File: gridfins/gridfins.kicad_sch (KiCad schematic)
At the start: 51 parts, among them J1 RBUS, U1 ESP32-S3, Y1 R940000171

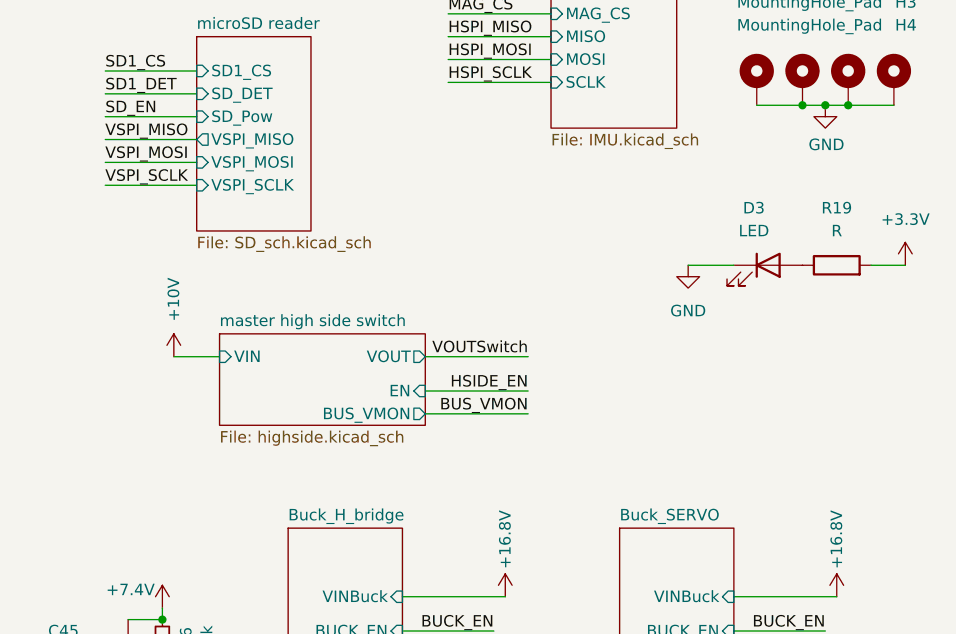
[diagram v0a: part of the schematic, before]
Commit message: PCB + schematic updates
Solved footprint error which prevented PCB from updating

Deleted old buck converter PCB design (old buck now replaced with 2 for servo and linear acc)

Moved Snubber and crossed out capacitor network to the backside of board

Unsure whether if the +10V routing is valid - currently connected via tracers, not planes (may be a problem for current)

Restructured old pcb which previously had planes associated with no nets (assigned nets to them)

If current design approved, will proceed to carry out the same design for the servo controlling buck converter.
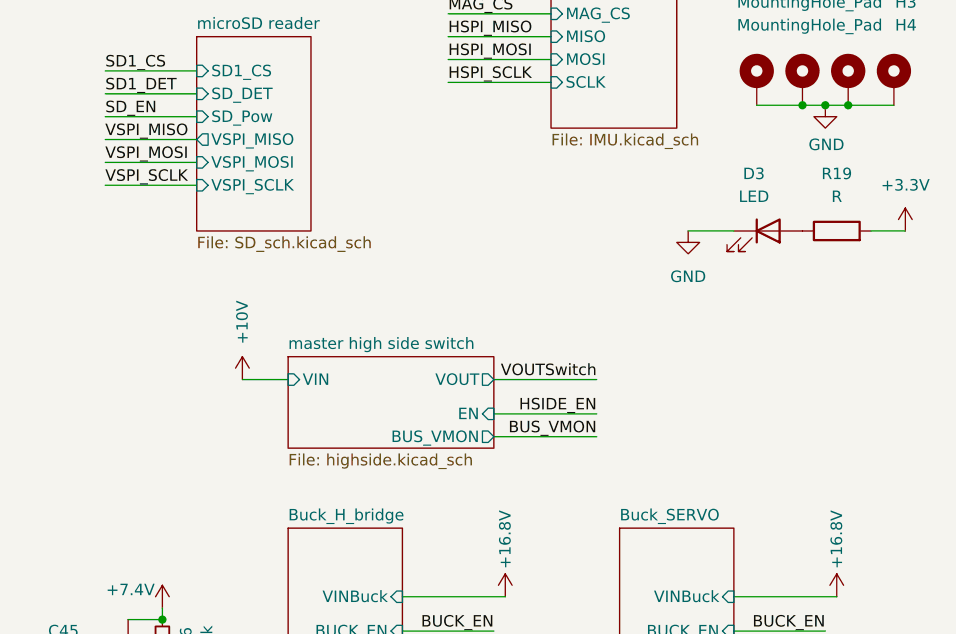
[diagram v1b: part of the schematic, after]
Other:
- moved on the sheet: D3, R19
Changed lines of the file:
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@@
 	(wire
 		(pts
-			(xy 226.06 67.31) (xy 237.49 67.31)
+			(xy 233.68 69.85) (xy 245.11 69.85)
 		)
 		(stroke
@@
 	(wire
 		(pts
-			(xy 255.27 50.8) (xy 260.35 50.8)
+			(xy 255.27 46.99) (xy 260.35 46.99)
 		)
 		(stroke
@@
 	(wire
 		(pts
-			(xy 226.06 60.96) (xy 237.49 60.96)
+			(xy 233.68 63.5) (xy 245.11 63.5)
 		)
 		(stroke
@@
 	(wire
 		(pts
-			(xy 279.4 50.8) (xy 275.59 50.8)
+			(xy 279.4 46.99) (xy 275.59 46.99)
 		)
 		(stroke
@@
 	(wire
 		(pts
-			(xy 198.12 60.96) (xy 203.2 60.96)
+			(xy 205.74 63.5) (xy 210.82 63.5)
 		)
 		(stroke
@@
 	(wire
 		(pts
-			(xy 226.06 64.77) (xy 237.49 64.77)
+			(xy 233.68 67.31) (xy 245.11 67.31)
 		)
 		(stroke
@@
 	)
 	(label "BUS_VMON"
-		(at 237.49 67.31 180)
+		(at 245.11 69.85 180)
 		(effects
 			(font
@@
 	)
 	(label "VOUTSwitch"
-		(at 237.49 60.96 180)
+		(at 245.11 63.5 180)
 		(effects
 			(font
@@
 	)
 	(label "HSIDE_EN"
-		(at 237.49 64.77 180)
+		(at 245.11 67.31 180)
 		(effects
 			(font
@@
 	(symbol
 		(lib_id "power:+3.3V")
-		(at 279.4 50.8 0)
+		(at 279.4 46.99 0)
 		(unit 1)
 		(exclude_from_sim no)
@@
 		(fields_autoplaced yes)
 		(property "Reference" "#PWR028"
-			(at 279.4 54.61 0)
+			(at 279.4 50.8 0)
 			(effects
 				(font
@@
 		)
 		(property "Value" "+3.3V"
-			(at 279.4 45.72 0)
+			(at 279.4 41.91 0)
 			(effects
 				(font
@@
 		)
 		(property "Footprint" ""
-			(at 279.4 50.8 0)
+			(at 279.4 46.99 0)
 			(effects
 				(font
@@
 		)
 		(property "Datasheet" ""
-			(at 279.4 50.8 0)
+			(at 279.4 46.99 0)
 			(effects
 				(font
@@
 		)
 		(property "Description" "Power symbol creates a global label with name \"+3.3V\""
-			(at 279.4 50.8 0)
+			(at 279.4 46.99 0)
 			(effects
 				(font
@@
 	(symbol
 		(lib_id "Device:R")
-		(at 271.78 50.8 90)
+		(at 271.78 46.99 90)
 		(unit 1)
 		(exclude_from_sim no)
@@
 		(dnp no)
 		(property "Reference" "R19"
-			(at 271.78 44.45 90)
+			(at 271.78 40.64 90)
 			(effects
 				(font
@@
 		)
 		(property "Value" "R"
-			(at 271.78 46.99 90)
+			(at 271.78 43.18 90)
 			(effects
 				(font
@@
 		)
 		(property "Footprint" "Resistor_SMD:R_0402_1005Metric"
-			(at 271.78 52.578 90)
+			(at 271.78 48.768 90)
 			(effects
 				(font
@@
 		)
 		(property "Datasheet" "~"
-			(at 271.78 50.8 0)
+			(at 271.78 46.99 0)
 			(effects
 				(font
@@
 		)
 		(property "Description" "Resistor"
-			(at 271.78 50.8 0)
+			(at 271.78 46.99 0)
 			(effects
 				(font
@@
 	(symbol
 		(lib_id "power:+12V")
-		(at 198.12 60.96 0)
+		(at 205.74 63.5 0)
 		(mirror y)
 		(unit 1)
@@
 		(dnp no)
 		(property "Reference" "#PWR062"
-			(at 198.12 64.77 0)
+			(at 205.74 67.31 0)
 			(effects
 				(font
@@
 		)
 		(property "Value" "+10V"
-			(at 198.12 54.61 90)
+			(at 205.74 57.15 90)
 			(effects
 				(font
@@
 		)
 		(property "Footprint" ""
-			(at 198.12 60.96 0)
+			(at 205.74 63.5 0)
 			(effects
 				(font
@@
 		)
 		(property "Datasheet" ""
-			(at 198.12 60.96 0)
+			(at 205.74 63.5 0)
 			(effects
 				(font
@@
 		)
 		(property "Description" "Power symbol creates a global label with name \"+12V\""
-			(at 198.12 60.96 0)
+			(at 205.74 63.5 0)
 			(effects
 				(font
@@
 	(symbol
 		(lib_id "power:GND")
-		(at 255.27 50.8 0)
+		(at 255.27 46.99 0)
 		(unit 1)
 		(exclude_from_sim no)
@@
 		(fields_autoplaced yes)
 		(property "Reference" "#PWR016"
-			(at 255.27 57.15 0)
+			(at 255.27 53.34 0)
 			(effects
 				(font
@@
 		)
 		(property "Value" "GND"
-			(at 255.27 55.88 0)
+			(at 255.27 52.07 0)
 			(effects
 				(font
@@
 		)
 		(property "Footprint" ""
-			(at 255.27 50.8 0)
+			(at 255.27 46.99 0)
 			(effects
 				(font
@@
 		)
 		(property "Datasheet" ""
-			(at 255.27 50.8 0)
+			(at 255.27 46.99 0)
 			(effects
 				(font
@@
 		)
 		(property "Description" "Power symbol creates a global label with name \"GND\" , ground"
-			(at 255.27 50.8 0)
+			(at 255.27 46.99 0)
 			(effects
 				(font
@@
 	(symbol
 		(lib_id "Device:LED")
-		(at 264.16 50.8 0)
+		(at 264.16 46.99 0)
 		(unit 1)
 		(exclude_from_sim no)
@@
 		(dnp no)
 		(property "Reference" "D3"
-			(at 262.5725 44.45 0)
+			(at 262.5725 40.64 0)
 			(effects
 				(font
@@
 		)
 		(property "Value" "LED"
-			(at 262.5725 46.99 0)
+			(at 262.5725 43.18 0)
 			(effects
 				(font
@@
 		)
 		(property "Footprint" "LED_SMD:LED_0402_1005Metric"
-			(at 264.16 50.8 0)
+			(at 264.16 46.99 0)
 			(effects
 				(font
@@
 		)
 		(property "Datasheet" "~"
-			(at 264.16 50.8 0)
+			(at 264.16 46.99 0)
 			(effects
 				(font
@@
 		)
 		(property "Description" "Light emitting diode"
-			(at 264.16 50.8 0)
+			(at 264.16 46.99 0)
 			(effects
 				(font
@@
 		)
 		(property "Sim.Pins" "1=K 2=A"
-			(at 264.16 50.8 0)
+			(at 264.16 46.99 0)
 			(effects
 				(font
@@
 	)
 	(sheet
-		(at 203.2 58.42)
+		(at 210.82 60.96)
 		(size 22.86 10.16)
 		(exclude_from_sim no)
@@
 		)
 		(property "Sheetname" "master high side switch"
-			(at 203.2 57.7084 0)
+			(at 210.82 60.2484 0)
 			(effects
 				(font
@@
 		)
 		(property "Sheetfile" "highside.kicad_sch"
-			(at 203.2 69.1646 0)
+			(at 210.82 71.7046 0)
 			(effects
 				(font
@@
 		)
 		(pin "BUS_VMON" output
-			(at 226.06 67.31 0)
+			(at 233.68 69.85 0)
 			(effects
 				(font
@@
 		)
 		(pin "EN" input
-			(at 226.06 64.77 0)
+			(at 233.68 67.31 0)
 			(effects
 				(font
@@
 		)
 		(pin "VIN" input
-			(at 203.2 60.96 180)
+			(at 210.82 63.5 180)
 			(effects
 				(font
@@
 		)
 		(pin "VOUT" output
-			(at 226.06 60.96 0)
+			(at 233.68 63.5 0)
 			(effects
 				(font

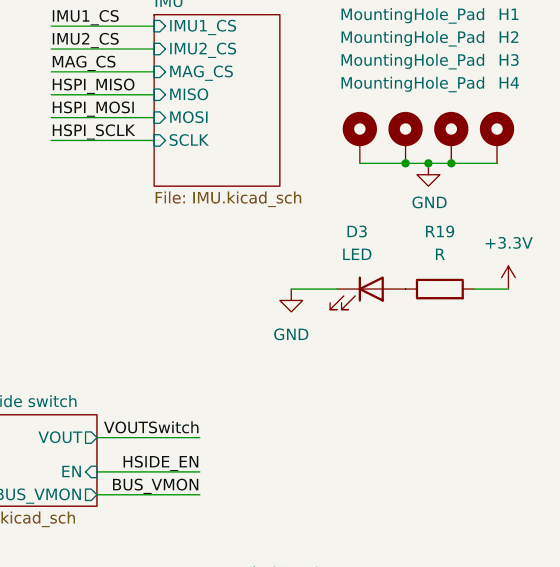
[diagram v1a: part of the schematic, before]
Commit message: Handoff
implemented changes advised by Will. Still a bit unsure about how the EPAD should be connected to ground. The PCB design of both buck converters for servo and Hbridge(linear accuator) was completed - but still needs to be reviewed
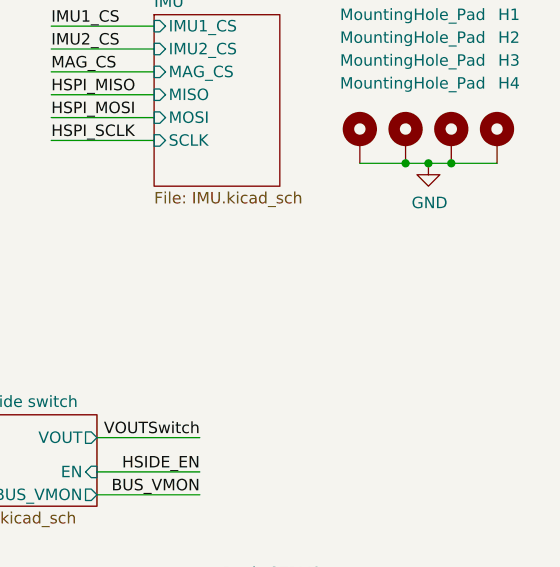
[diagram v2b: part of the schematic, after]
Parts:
- removed D3: LED, LED_SMD:LED_0402_1005Metric, symbol Device:LED
- removed R19: R, Resistor_SMD:R_0402_1005Metric, symbol Device:R
